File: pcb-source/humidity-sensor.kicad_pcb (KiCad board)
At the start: 2 copper layers, 34.3 x 22.6 mm, 77 parts, among them J1 Conn_ARM_JTAG_SWD_10, J2 Conn_02x03_Odd_Even, Q1 Q_NMOS_GSD, Q2 Q_NMOS_GSD, U1 STM32L051C8Tx, U2 SHTC3, U3 SYN115, Y1 13.56MHz, Y2 DNU

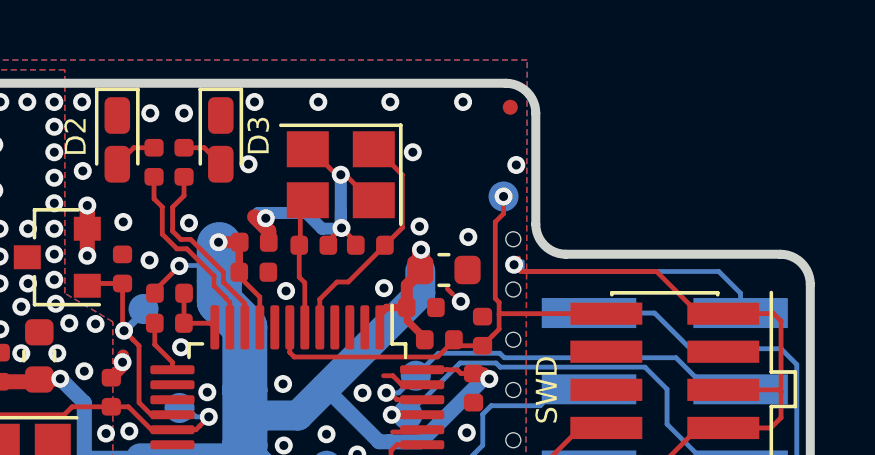
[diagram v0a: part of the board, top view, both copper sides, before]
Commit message: Add 1.2mm NPTH for alignment
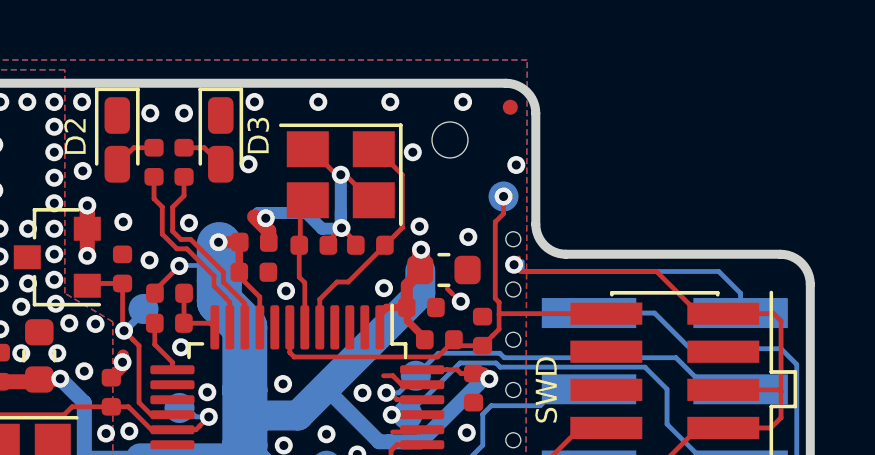
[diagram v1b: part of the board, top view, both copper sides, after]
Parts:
- added REF**: NPTH-1.2mm, NPTH:NPTH-1.2mm, F.Cu at (76.9, 29.2)
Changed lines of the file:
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@@
     (tracks 759)
     (zones 0)
-    (modules 77)
+    (modules 78)
     (nets 55)
   )
@@
   (layers
     (0 F.Cu signal)
-    (31 B.Cu signal)
+    (31 B.Cu signal hide)
     (32 B.Adhes user hide)
     (33 F.Adhes user hide)
     (34 B.Paste user hide)
     (35 F.Paste user hide)
-    (36 B.SilkS user hide)
+    (36 B.SilkS user)
     (37 F.SilkS user)
     (38 B.Mask user hide)
@@
     (add_net VCC)
   )
+  (module NPTH:NPTH-1.2mm (layer F.Cu)
+    (at 76.89 29.19)
+    (fp_text reference REF** (at 0.3 1.85) (layer F.SilkS) hide
+      (effects (font (size 1 1) (thickness 0.15)))
+    )
+    (fp_text value NPTH-1.2mm (at 0.6 -1.5) (layer F.Fab) hide
+      (effects (font (size 1 1) (thickness 0.15)))
+    )
+    (fp_circle (center 0 0) (end 0.85 0) (layer F.CrtYd) (width 0.05))
+    (pad "" np_thru_hole circle (at 0 0) (size 1.2 1.2) (drill 1.2) (layers *.Cu *.Mask))
+  )
   (module Symbol:OSHW-Symbol_6.7x6mm_Copper (layer B.Cu)

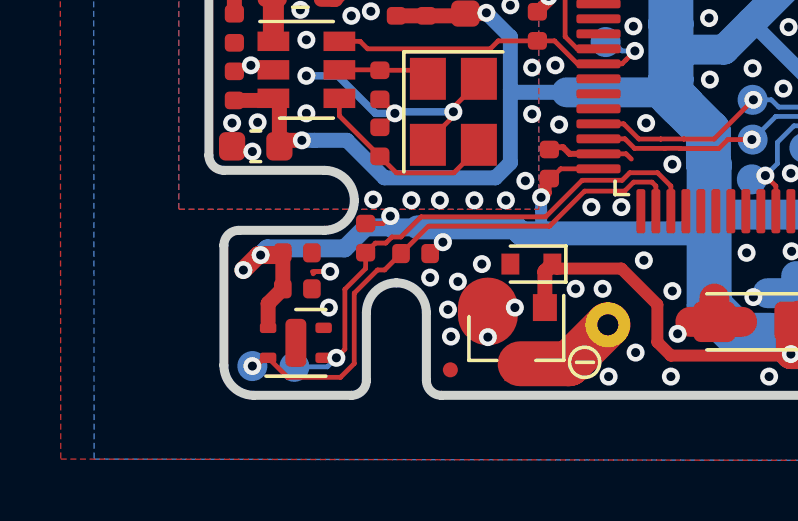
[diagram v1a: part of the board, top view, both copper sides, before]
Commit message: Modify fiducials
Library footprint doesn't create copper pull-back from
soldermask opening.
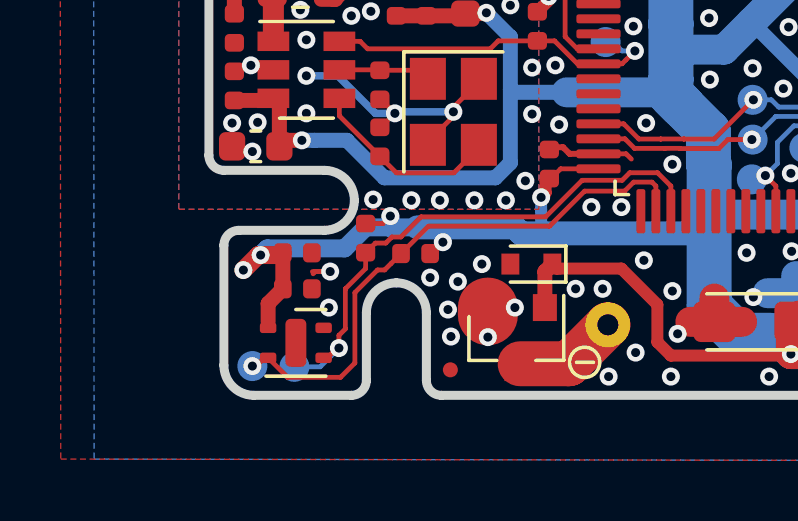
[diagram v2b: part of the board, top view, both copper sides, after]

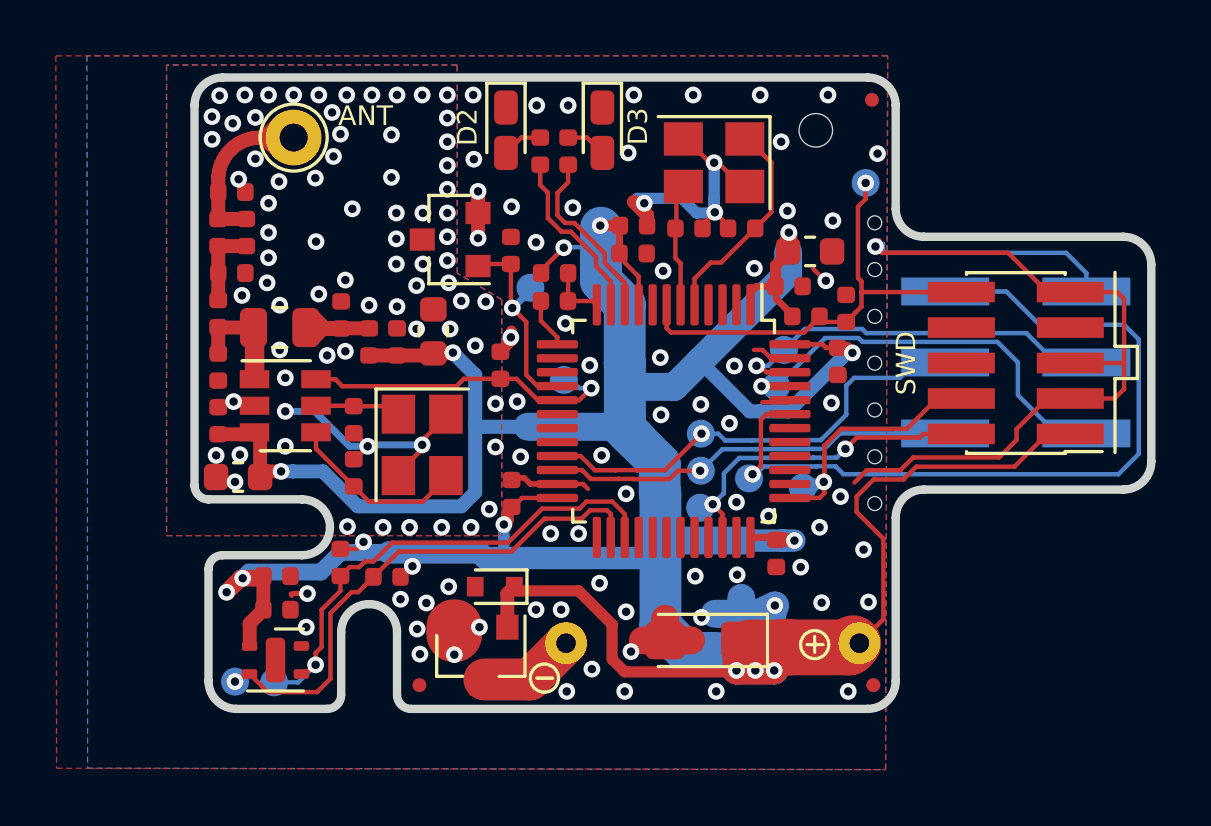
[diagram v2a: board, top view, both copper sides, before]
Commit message: Update revision, beef trace, clean GND
- Change from rev '0.1.0' to 'r0.1'.
- Beef up GND trace for humidity sensor.
- Tidy GND pours/traces.
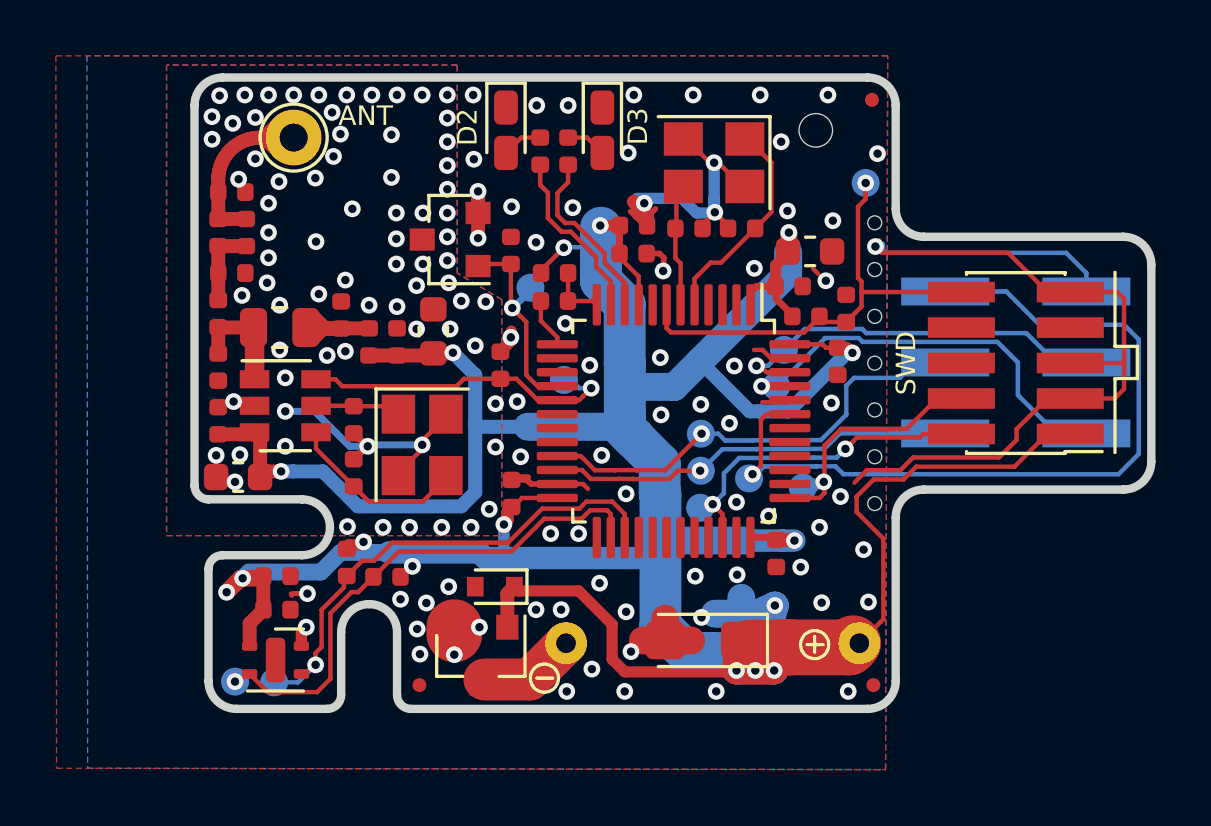
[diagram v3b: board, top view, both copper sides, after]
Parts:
- moved R7 0.23 mm to (60.1, 44.7)
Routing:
- net GND: track 63.8 -> 68.6 mm
- net GNDA: track 9.73 -> 10.4 mm
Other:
- board text added: "r0.1"
- board text removed: "0.1.0"

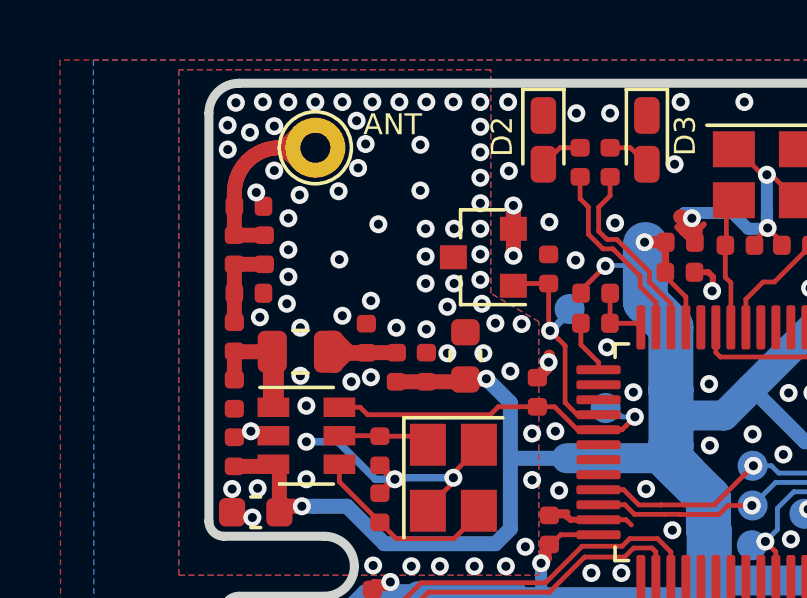
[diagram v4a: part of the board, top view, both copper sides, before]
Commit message: Generate modified footprint library
- Altered 3D filepath
- Add generated directory to .gitignore
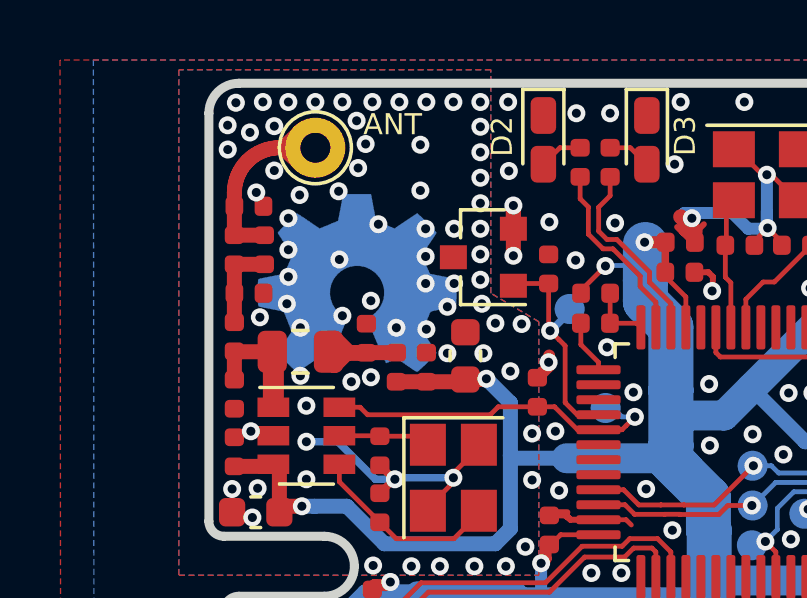
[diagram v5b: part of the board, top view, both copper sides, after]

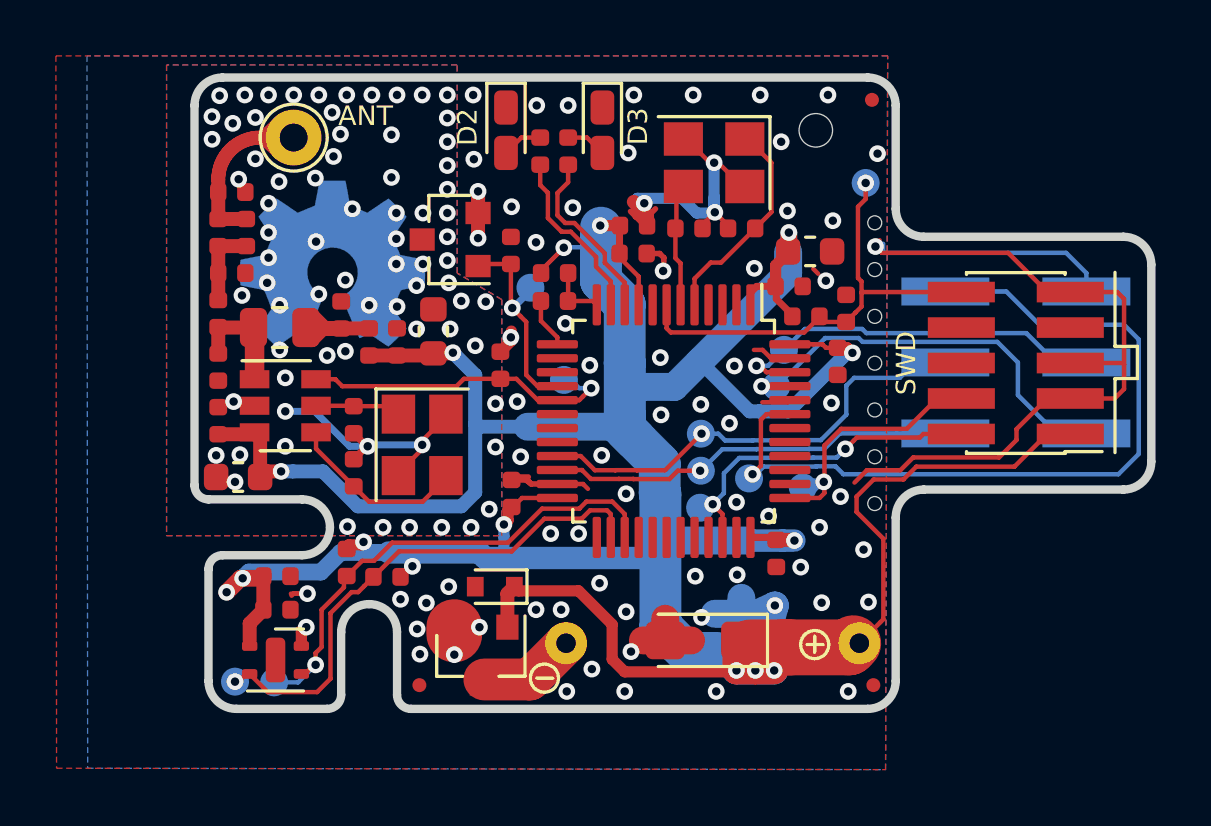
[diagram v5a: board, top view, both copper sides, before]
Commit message: Update XTAL GND
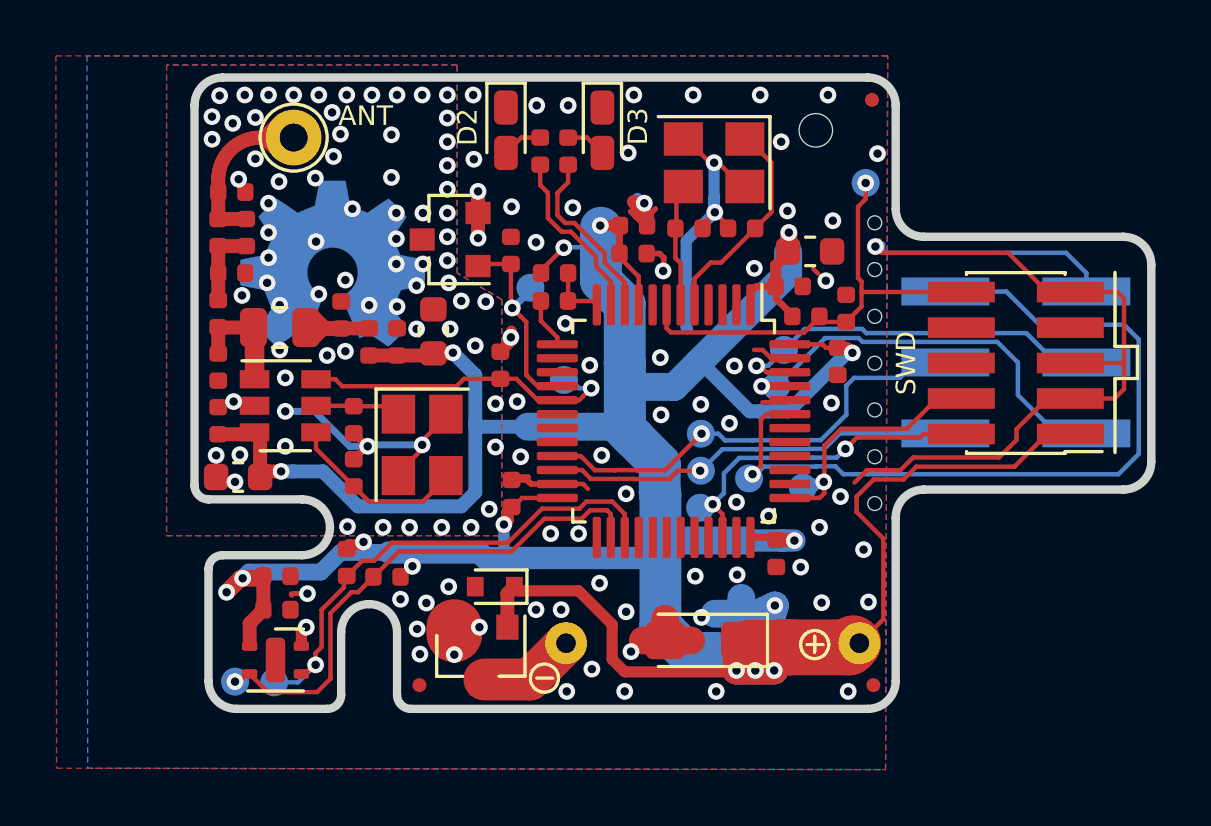
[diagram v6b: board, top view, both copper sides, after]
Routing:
- net GND: track 68.6 -> 70.3 mm
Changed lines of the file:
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@@
   (segment (start 58.125 45.85) (end 58.2 45.775) (width 0.16) (layer F.Cu) (net 25))
   (segment (start 73.25 32.1) (end 73.25 31.575) (width 0.4) (layer B.Cu) (net 25))
-  (segment (start 72.1 31.625) (end 70.5 31.625) (width 0.4) (layer B.Cu) (net 25))
   (segment (start 73.25 32.1) (end 73.2 32.15) (width 0.4) (layer B.Cu) (net 25))
   (segment (start 70.5 31.625) (end 70.375 31.75) (width 0.4) (layer B.Cu) (net 25))
-  (segment (start 72.625 32.15) (end 72.1 31.625) (width 0.4) (layer B.Cu) (net 25))
-  (segment (start 73.2 32.15) (end 72.625 32.15) (width 0.4) (layer B.Cu) (net 25))
   (segment (start 78.717599 41.357401) (end 78.275 41.8) (width 0.16) (layer F.Cu) (net 25))
   (segment (start 79.917777 41.357401) (end 78.717599 41.357401) (width 0.16) (layer F.Cu) (net 25))
@@
   (segment (start 66.105 41.6) (end 66.6 41.6) (width 0.2) (layer F.Cu) (net 25))
   (segment (start 66 41.705) (end 66.105 41.6) (width 0.2) (layer F.Cu) (net 25))
+  (segment (start 73.275 32.125) (end 72.25 33.15) (width 0.4) (layer B.Cu) (net 25))
+  (segment (start 72.25 36.25) (end 72.3 36.3) (width 0.4) (layer B.Cu) (net 25))
+  (segment (start 72.25 33.15) (end 72.25 36.25) (width 0.4) (layer B.Cu) (net 25))
   (segment (start 66.65241 48.84759) (end 65.025 48.84759) (width 1.5) (layer F.Cu) (net 29))
   (segment (start 67.95 47.55) (end 66.65241 48.84759) (width 1.5) (layer F.Cu) (net 29))

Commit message: Revert OSHW logo to soldermask layer
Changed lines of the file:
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@@
     (add_net VCC)
-  )
-  (module Fiducial:Fiducial_0.5mm_Mask1mm (layer F.Cu)
-    (at 78.9 28.1)
-    (descr "Circular Fiducial, 0.5mm bare copper, 1mm soldermask opening (Level C)")
-    (tags fiducial)
-    (attr smd)
-    (fp_text reference FID3 (at 0 -1.5) (layer F.SilkS) hide
-      (effects (font (size 1 1) (thickness 0.15)))
-    )
-    (fp_text value Fiducial (at 0 1.5) (layer F.Fab) hide
-      (effects (font (size 1 1) (thickness 0.15)))
-    )
-    (fp_circle (center 0 0) (end 0.75 0) (layer F.CrtYd) (width 0.05))
-    (fp_text user %R (at 0 0) (layer F.Fab)
-      (effects (font (size 0.2 0.2) (thickness 0.04)))
-    )
-    (fp_circle (center 0 0) (end 0.5 0) (layer F.Fab) (width 0.1))
-    (pad "" smd circle (at 0 0) (size 0.5 0.5) (layers F.Cu F.Mask)
-      (solder_mask_margin 0.25) (clearance 0.25))
-  )
-  (module Fiducial:Fiducial_0.5mm_Mask1mm (layer F.Cu)
-    (at 78.95 49.05)
-    (descr "Circular Fiducial, 0.5mm bare copper, 1mm soldermask opening (Level C)")
-    (tags fiducial)
-    (attr smd)
-    (fp_text reference FID2 (at 0 -1.5) (layer F.SilkS) hide
-      (effects (font (size 1 1) (thickness 0.15)))
-    )
-    (fp_text value Fiducial (at 0 1.5) (layer F.Fab) hide
-      (effects (font (size 1 1) (thickness 0.15)))
-    )
-    (fp_circle (center 0 0) (end 0.75 0) (layer F.CrtYd) (width 0.05))
-    (fp_text user %R (at 0 0) (layer F.Fab)
-      (effects (font (size 0.2 0.2) (thickness 0.04)))
-    )
-    (fp_circle (center 0 0) (end 0.5 0) (layer F.Fab) (width 0.1))
-    (pad "" smd circle (at 0 0) (size 0.5 0.5) (layers F.Cu F.Mask)
-      (solder_mask_margin 0.25) (clearance 0.25))
-  )
-  (module Fiducial:Fiducial_0.5mm_Mask1mm (layer F.Cu)
-    (at 62.7 49.05)
-    (descr "Circular Fiducial, 0.5mm bare copper, 1mm soldermask opening (Level C)")
-    (tags fiducial)
-    (attr smd)
-    (fp_text reference FID1 (at 0 -1.5) (layer F.SilkS) hide
-      (effects (font (size 1 1) (thickness 0.15)))
-    )
-    (fp_text value Fiducial (at 0 1.5) (layer F.Fab) hide
-      (effects (font (size 1 1) (thickness 0.15)))
-    )
-    (fp_circle (center 0 0) (end 0.75 0) (layer F.CrtYd) (width 0.05))
-    (fp_text user %R (at 0 0) (layer F.Fab)
-      (effects (font (size 0.2 0.2) (thickness 0.04)))
-    )
-    (fp_circle (center 0 0) (end 0.5 0) (layer F.Fab) (width 0.1))
-    (pad "" smd circle (at 0 0) (size 0.5 0.5) (layers F.Cu F.Mask)
-      (solder_mask_margin 0.25) (clearance 0.25))
   )
   (module Symbol:OSHW-Symbol_6.7x6mm_Copper (layer B.Cu)
@@
     (tags "Logo Symbol OSHW")
     (attr virtual)
-    (fp_text reference REF** (at 0 0) (layer B.SilkS) hide
+    (fp_text reference REF** (at 0 0 180) (layer B.SilkS) hide
       (effects (font (size 1 1) (thickness 0.15)) (justify mirror))
     )
-    (fp_text value OSHW-Symbol_6.7x6mm_Copper (at 0.75 0) (layer B.Fab) hide
+    (fp_text value OSHW-Symbol_6.7x6mm_Copper (at 0.75 0 180) (layer B.Fab) hide
       (effects (font (size 1 1) (thickness 0.15)) (justify mirror))
     )
@@
       (xy -1.781499 2.198782) (xy -1.684144 2.133494) (xy -1.610707 2.083754) (xy -1.239667 1.831449)
       (xy -0.621095 2.086445) (xy -0.537275 2.531069) (xy -0.453454 2.975693) (xy 0.471994 2.975693)
-      (xy 0.555814 2.531069)) (layer B.Cu) (width 0.01))
+      (xy 0.555814 2.531069)) (layer B.Mask) (width 0.01))
+  )
+  (module Fiducial:Fiducial_0.5mm_Mask1mm (layer F.Cu)
+    (at 78.9 28.1)
+    (descr "Circular Fiducial, 0.5mm bare copper, 1mm soldermask opening (Level C)")
+    (tags fiducial)
+    (attr smd)
+    (fp_text reference FID3 (at 0 -1.5) (layer F.SilkS) hide
+      (effects (font (size 1 1) (thickness 0.15)))
+    )
+    (fp_text value Fiducial (at 0 1.5) (layer F.Fab) hide
+      (effects (font (size 1 1) (thickness 0.15)))
+    )
+    (fp_circle (center 0 0) (end 0.75 0) (layer F.CrtYd) (width 0.05))
+    (fp_text user %R (at 0 0) (layer F.Fab)
+      (effects (font (size 0.2 0.2) (thickness 0.04)))
+    )
+    (fp_circle (center 0 0) (end 0.5 0) (layer F.Fab) (width 0.1))
+    (pad "" smd circle (at 0 0) (size 0.5 0.5) (layers F.Cu F.Mask)
+      (solder_mask_margin 0.25) (clearance 0.25))
+  )
+  (module Fiducial:Fiducial_0.5mm_Mask1mm (layer F.Cu)
+    (at 78.95 49.05)
+    (descr "Circular Fiducial, 0.5mm bare copper, 1mm soldermask opening (Level C)")
+    (tags fiducial)
+    (attr smd)
+    (fp_text reference FID2 (at 0 -1.5) (layer F.SilkS) hide
+      (effects (font (size 1 1) (thickness 0.15)))
+    )
+    (fp_text value Fiducial (at 0 1.5) (layer F.Fab) hide
+      (effects (font (size 1 1) (thickness 0.15)))
+    )
+    (fp_circle (center 0 0) (end 0.75 0) (layer F.CrtYd) (width 0.05))
+    (fp_text user %R (at 0 0) (layer F.Fab)
+      (effects (font (size 0.2 0.2) (thickness 0.04)))
+    )
+    (fp_circle (center 0 0) (end 0.5 0) (layer F.Fab) (width 0.1))
+    (pad "" smd circle (at 0 0) (size 0.5 0.5) (layers F.Cu F.Mask)
+      (solder_mask_margin 0.25) (clearance 0.25))
+  )
+  (module Fiducial:Fiducial_0.5mm_Mask1mm (layer F.Cu)
+    (at 62.7 49.05)
+    (descr "Circular Fiducial, 0.5mm bare copper, 1mm soldermask opening (Level C)")
+    (tags fiducial)
+    (attr smd)
+    (fp_text reference FID1 (at 0 -1.5) (layer F.SilkS) hide
+      (effects (font (size 1 1) (thickness 0.15)))
+    )
+    (fp_text value Fiducial (at 0 1.5) (layer F.Fab) hide
+      (effects (font (size 1 1) (thickness 0.15)))
+    )
+    (fp_circle (center 0 0) (end 0.75 0) (layer F.CrtYd) (width 0.05))
+    (fp_text user %R (at 0 0) (layer F.Fab)
+      (effects (font (size 0.2 0.2) (thickness 0.04)))
+    )
+    (fp_circle (center 0 0) (end 0.5 0) (layer F.Fab) (width 0.1))
+    (pad "" smd circle (at 0 0) (size 0.5 0.5) (layers F.Cu F.Mask)
+      (solder_mask_margin 0.25) (clearance 0.25))
   )
   (module TestPoint:TestPoint_Pad_D1.0mm (layer B.Cu)
